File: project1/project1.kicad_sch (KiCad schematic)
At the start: 30 parts, among them J1 Barrel_Jack, J2 Conn_01x04, J3 Conn_01x02, J4 Conn_01x02, J5 Conn_01x02, J6 Conn_01x02, Q1 NMOS, Q2 S8550, SW1 SW_SPST, U1 HX711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

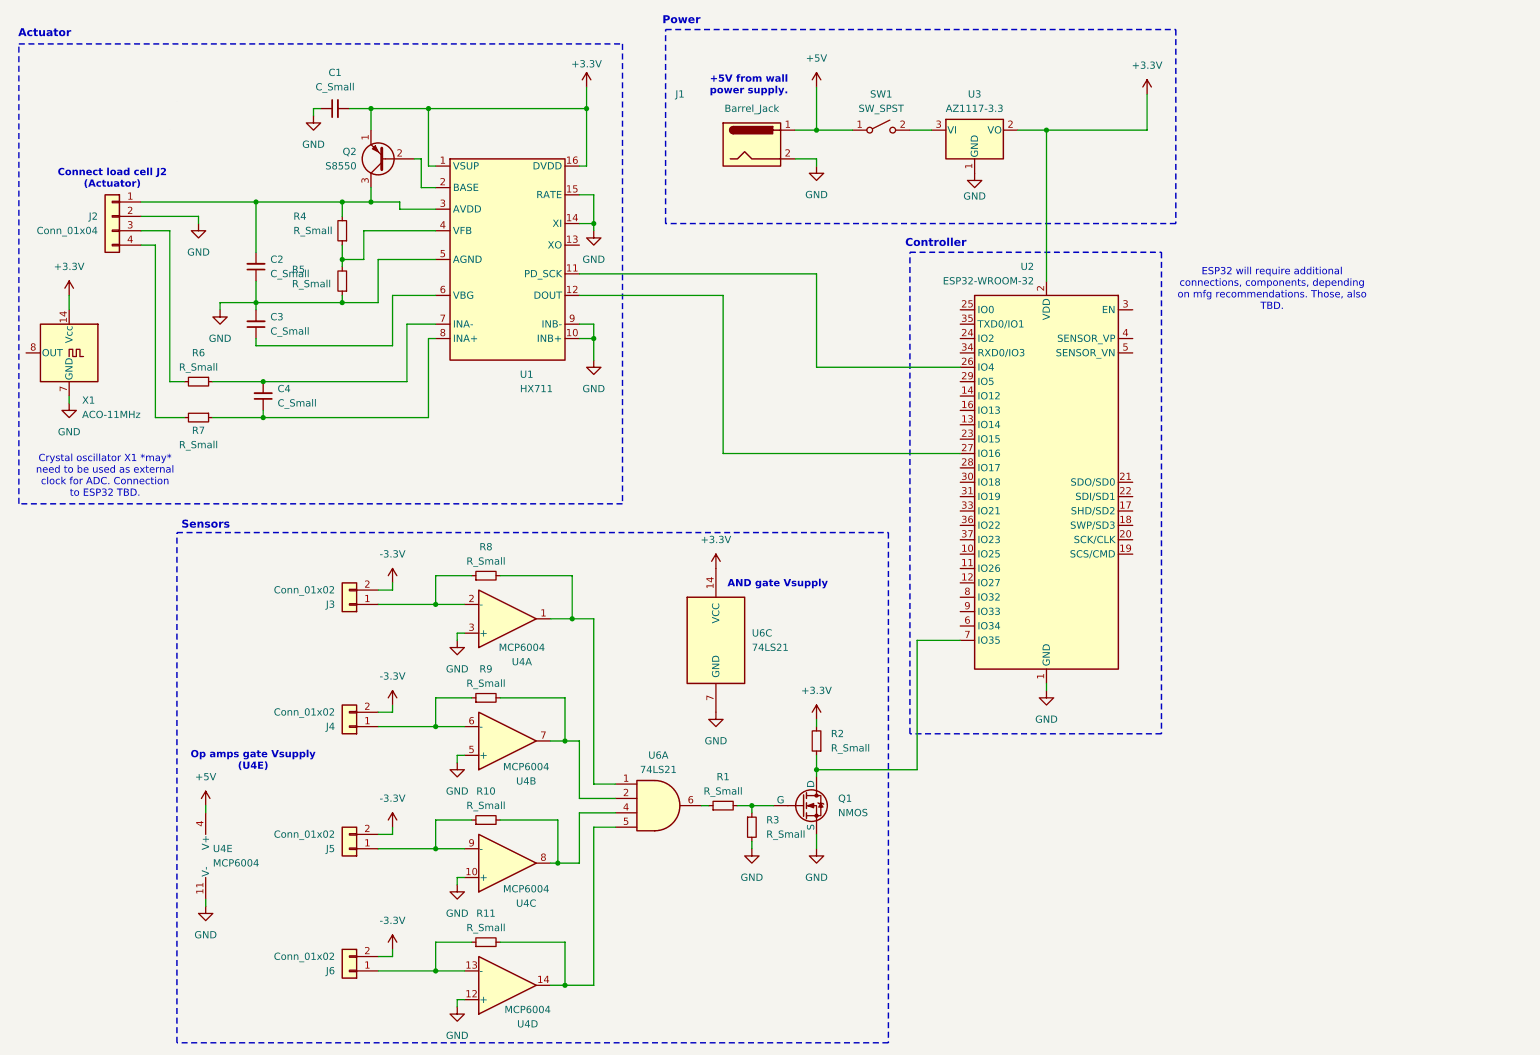
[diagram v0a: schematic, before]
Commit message: Stu schem update (#23)
* adding outline for gantt chart update

* update schematic, added footprints, started layout.
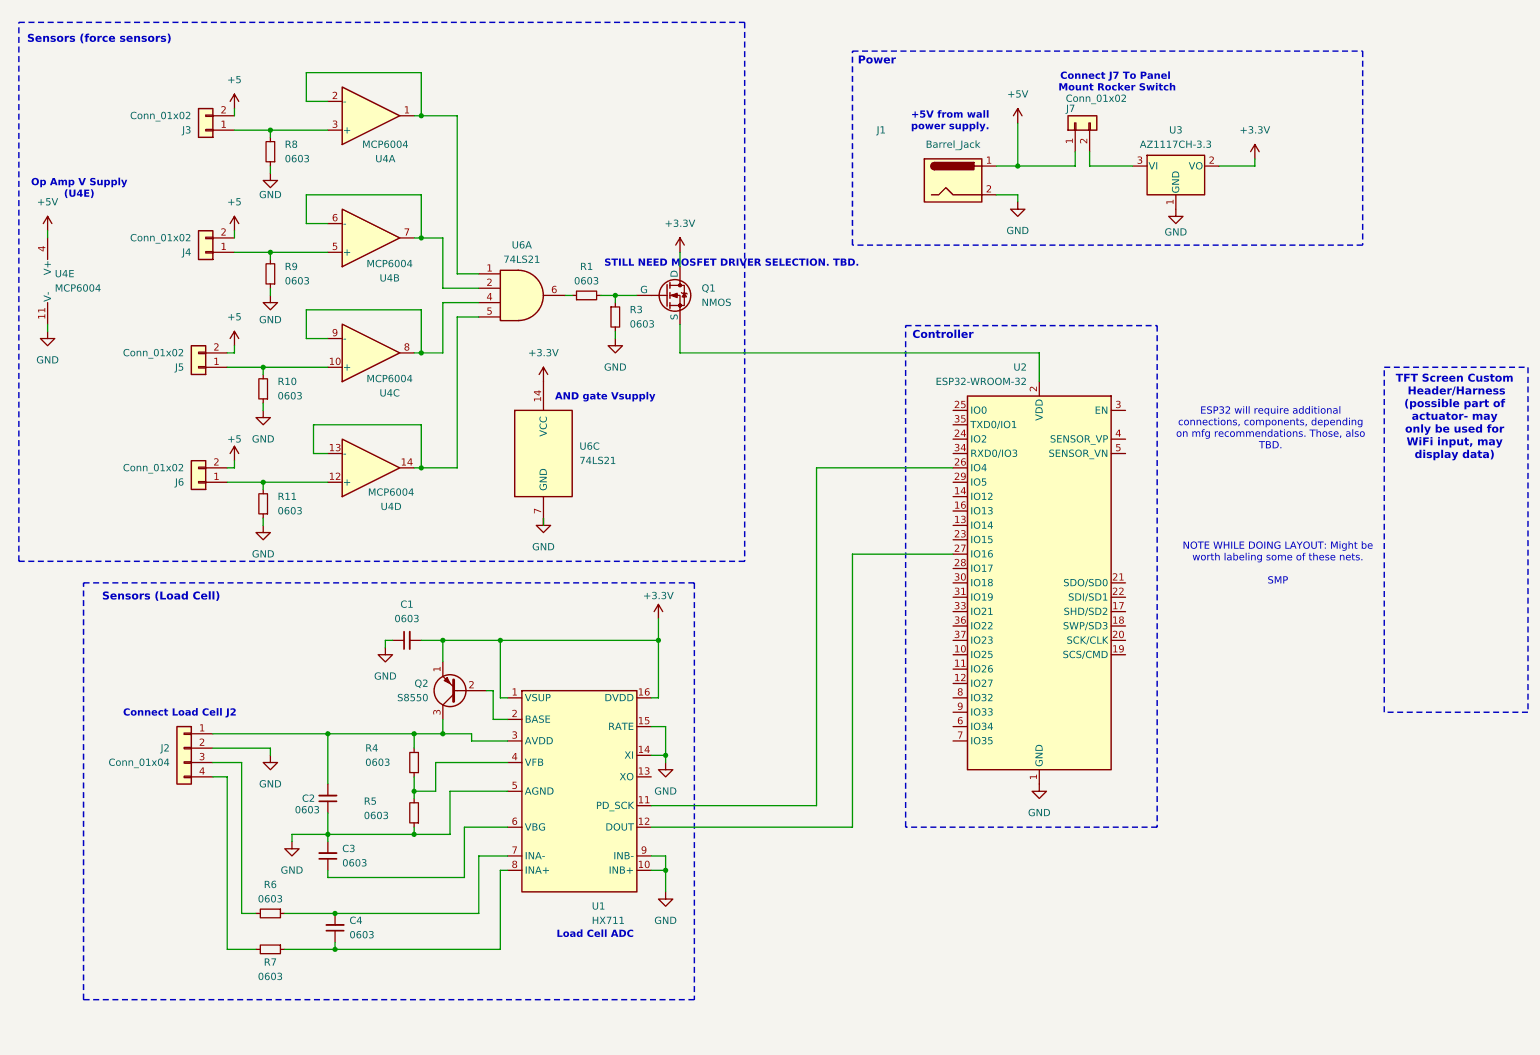
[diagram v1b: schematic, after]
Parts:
- removed R2: R_Small, symbol Device:R_Small
- removed SW1: SW_SPST, symbol Switch:SW_SPST
- removed X1: ACO-11MHz, Oscillator:Oscillator_DIP-14, symbol Oscillator:ACO-xxxMHz
- added J7: Conn_01x02, Connector_JST:JST_XA_S02B-XASK-1_1x02_P2.50mm_Horizontal, symbol Connector_Generic:Conn_01x02
- C1, C2, C3, C4: value C_Small -> 0603; footprint (none) -> Capacitor_SMD:C_0201_0603Metric
- J1: footprint (none) -> Connector_BarrelJack:BarrelJack_Kycon_KLDX-0202-xC_Horizontal
- J2: footprint (none) -> Connector_JST:JST_XA_S04B-XASK-1N-BN_1x04_P2.50mm_Horizontal
- J3, J4, J5, J6: footprint (none) -> Connector_JST:JST_XA_S02B-XASK-1_1x02_P2.50mm_Horizontal
- Q1: footprint (none) -> Package_TO_SOT_SMD:SOT-323_SC-70
- Q2: footprint Package_TO_SOT_THT:TO-92_Inline -> Package_TO_SOT_SMD:SOT-23-3
- R1, R3: value R_Small -> 0603
- R10, R11, R4, R5, R6, R7, R8, R9: value R_Small -> 0603; footprint (none) -> Resistor_SMD:R_0201_0603Metric
- U3: value AZ1117-3.3 -> AZ1117CH-3.3; footprint (none) -> Package_TO_SOT_SMD:SOT-223
- U4: footprint (none) -> Package_SO:SOIC-14_3.9x8.7mm_P1.27mm
- U6: footprint (none) -> Package_SO:SO-14_5.3x10.2mm_P1.27mm
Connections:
- net +3.3V: now also Q1.1 (D); no longer U2.2 (VDD)
- net +5V: now also J7.1 (Pin_1)
- net GND: now also R10.1, R11.1, R8.1, R9.1; no longer Q1.3 (S), U4.10 (+), U4.12 (+), U4.3 (+), U4.5 (+)
- net at U4.7, U6.2: now also U4.6 (-); no longer R9.2
- net at U2.7 (IO35): no longer Q1.1 (D)
- net at U4.8, U6.4: now also U4.9 (-); no longer R10.2
- net at U4.14, U6.5: now also U4.13 (-); no longer R11.2
- net at U4.1, U6.1: now also U4.2 (-); no longer R8.2
- net at U3.3 (VI): now also J7.2 (Pin_2)
- net -3.3V renamed +5
- new net: J4.1 (Pin_1), R9.2, U4.5 (+)
- new net: J5.1 (Pin_1), R10.2, U4.10 (+)
- new net: Q1.3 (S), U2.2 (VDD)
- new net: J3.1 (Pin_1), R8.2, U4.3 (+)
- new net: J6.1 (Pin_1), R11.2, U4.12 (+)
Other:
- note added: "Connect J7 To Panel Mount Rocker Switch"
- note added: "Connect Load Cell J2"
- note added: "Load Cell ADC"
- note added: "NOTE WHILE DOING LAYOUT: Might be worth labeling some of these nets. SMP"
- note added: "Op Amp V Supply (U4E)"
- note added: "STILL NEED MOSFET DRIVER SELECTION. TBD."
- note added: "Sensors (Load Cell)"
- note added: "Sensors (force sensors)"
- note added: "TFT Screen Custom Header/Harness (possible part of actuator- may only be used for WiFi input, may display data)"
- note removed: "Actuator"
- note removed: "Connect load cell J2 (Actuator)"
- note removed: "Crystal oscillator X1 *may* need to be used as external clock for ADC. Connection to ESP32 TBD."
- note removed: "Op amps gate Vsupply (U4E)"
- note removed: "Sensors"
- moved on the sheet: C1, C2, C3, C4, J1, J2, J3, Q1, Q2, R1, R3, R4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
